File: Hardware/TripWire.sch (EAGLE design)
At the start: 50 parts, among them P1 LSP11, P2 LSP11, P3 LSP11, P4 LSP11, P5 LSP11, P6 LSP11, P7 LSP11, X1 GADGETEER-SOCKET

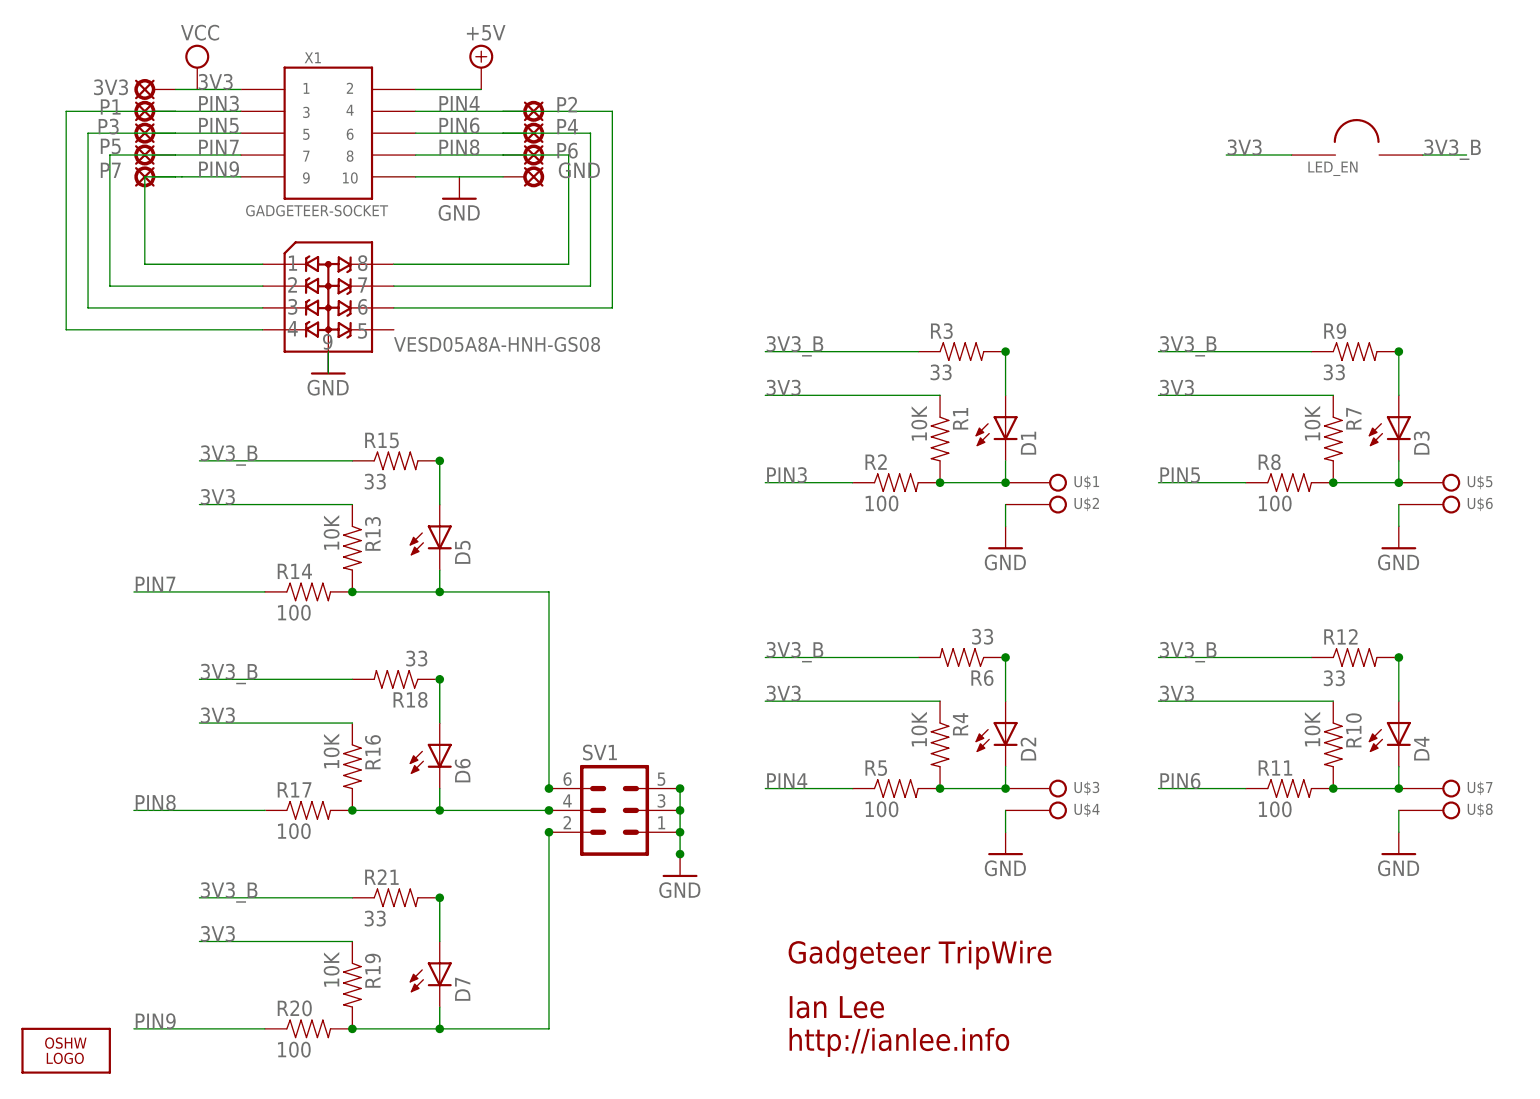
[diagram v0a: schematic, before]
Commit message: Adjusted text sizes & placement.
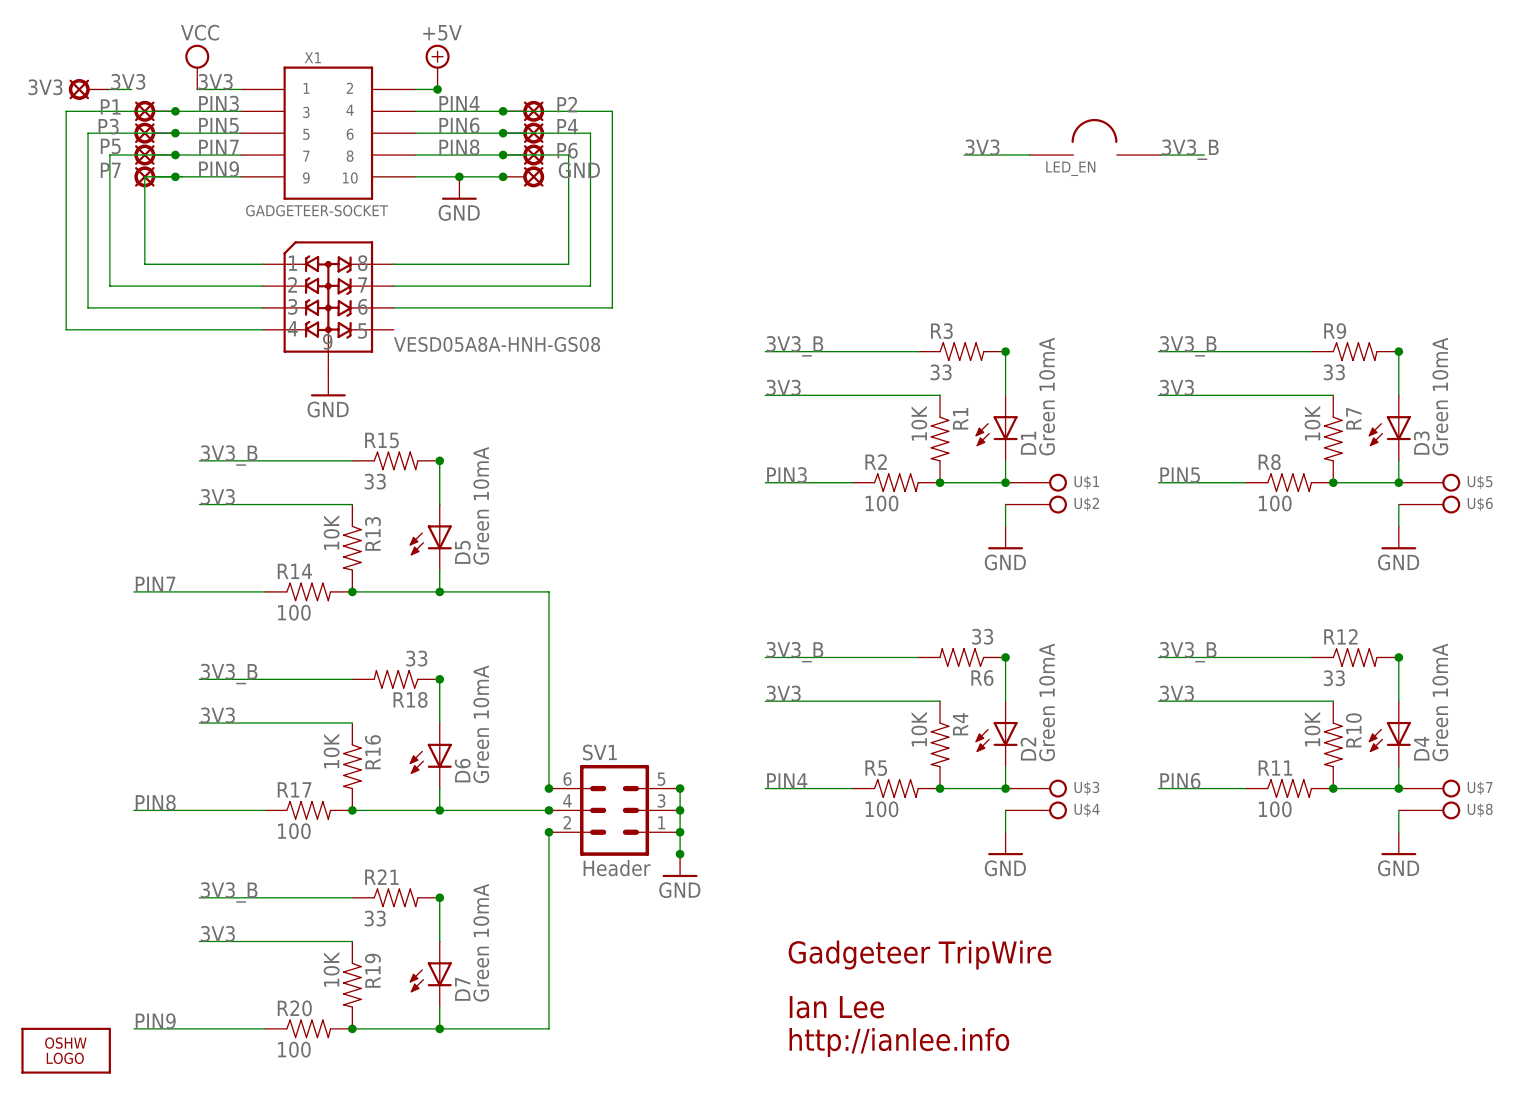
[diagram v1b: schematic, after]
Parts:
- D1, D2, D3, D4, D5, D6, D7: value (none) -> Green 10mA
- SV1: value (none) -> Header
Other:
- moved on the sheet: 3V3, LED_EN
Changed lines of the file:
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@@
 <setting verticaltext="up"/>
 </settings>
-<grid distance="0.1" unitdist="inch" unit="mm" style="lines" multiple="1" display="no" altdistance="0.01" altunitdist="inch" altunit="mm"/>
+<grid distance="0.1" unitdist="inch" unit="inch" style="lines" multiple="1" display="no" altdistance="0.01" altunitdist="inch" altunit="inch"/>
 <layers>
 <layer number="1" name="Top" color="4" fill="1" visible="no" active="no"/>
@@
 </variantdefs>
 <classes>
-<class number="0" name="default" width="0.254" drill="0.381">
+<class number="0" name="default" width="0.1524" drill="0.254">
 <clearance class="0" value="0.2032"/>
 </class>
@@
 <part name="FRAME2" library="frames" deviceset="A5L-LOC" device=""/>
 <part name="GND1" library="supply1" deviceset="GND" device=""/>
-<part name="V1" library="supply2" deviceset="+5V" device=""/>
 <part name="V2" library="supply2" deviceset="VCC" device=""/>
 <part name="X1" library="SoftDust" deviceset="GADGETEER-SOCKET" device=""/>
@@
 <part name="GND5" library="supply1" deviceset="GND" device=""/>
 <part name="GND6" library="supply1" deviceset="GND" device=""/>
-<part name="SV1" library="con-lstb" deviceset="MA03-2" device=""/>
-<part name="D1" library="SparkFun-LED" deviceset="LED-YELLOW" device="0603"/>
+<part name="SV1" library="con-lstb" deviceset="MA03-2" device="" value="Header"/>
+<part name="D1" library="SparkFun-LED" deviceset="LED-YELLOW" device="0603" value="Green 10mA"/>
 <part name="R1" library="SparkFun-Resistors" deviceset="RESISTOR" device="0603-RES" value="10K"/>
 <part name="R2" library="SparkFun-Resistors" deviceset="RESISTOR" device="0603-RES" value="100"/>
 <part name="R3" library="SparkFun-Resistors" deviceset="RESISTOR" device="0603-RES" value="33"/>
-<part name="D2" library="SparkFun-LED" deviceset="LED-YELLOW" device="0603"/>
+<part name="D2" library="SparkFun-LED" deviceset="LED-YELLOW" device="0603" value="Green 10mA"/>
 <part name="R4" library="SparkFun-Resistors" deviceset="RESISTOR" device="0603-RES" value="10K"/>
 <part name="R5" library="SparkFun-Resistors" deviceset="RESISTOR" device="0603-RES" value="100"/>
 <part name="R6" library="SparkFun-Resistors" deviceset="RESISTOR" device="0603-RES" value="33"/>
-<part name="D3" library="SparkFun-LED" deviceset="LED-YELLOW" device="0603"/>
+<part name="D3" library="SparkFun-LED" deviceset="LED-YELLOW" device="0603" value="Green 10mA"/>
 <part name="R7" library="SparkFun-Resistors" deviceset="RESISTOR" device="0603-RES" value="10K"/>
 <part name="R8" library="SparkFun-Resistors" deviceset="RESISTOR" device="0603-RES" value="100"/>
 <part name="R9" library="SparkFun-Resistors" deviceset="RESISTOR" device="0603-RES" value="33"/>
-<part name="D4" library="SparkFun-LED" deviceset="LED-YELLOW" device="0603"/>
+<part name="D4" library="SparkFun-LED" deviceset="LED-YELLOW" device="0603" value="Green 10mA"/>
 <part name="R10" library="SparkFun-Resistors" deviceset="RESISTOR" device="0603-RES" value="10K"/>
 <part name="R11" library="SparkFun-Resistors" deviceset="RESISTOR" device="0603-RES" value="100"/>
 <part name="R12" library="SparkFun-Resistors" deviceset="RESISTOR" device="0603-RES" value="33"/>
-<part name="D5" library="SparkFun-LED" deviceset="LED-YELLOW" device="0603"/>
+<part name="D5" library="SparkFun-LED" deviceset="LED-YELLOW" device="0603" value="Green 10mA"/>
 <part name="R13" library="SparkFun-Resistors" deviceset="RESISTOR" device="0603-RES" value="10K"/>
 <part name="R14" library="SparkFun-Resistors" deviceset="RESISTOR" device="0603-RES" value="100"/>
 <part name="R15" library="SparkFun-Resistors" deviceset="RESISTOR" device="0603-RES" value="33"/>
-<part name="D6" library="SparkFun-LED" deviceset="LED-YELLOW" device="0603"/>
+<part name="D6" library="SparkFun-LED" deviceset="LED-YELLOW" device="0603" value="Green 10mA"/>
 <part name="R16" library="SparkFun-Resistors" deviceset="RESISTOR" device="0603-RES" value="10K"/>
 <part name="R17" library="SparkFun-Resistors" deviceset="RESISTOR" device="0603-RES" value="100"/>
 <part name="R18" library="SparkFun-Resistors" deviceset="RESISTOR" device="0603-RES" value="33"/>
-<part name="D7" library="SparkFun-LED" deviceset="LED-YELLOW" device="0603"/>
+<part name="D7" library="SparkFun-LED" deviceset="LED-YELLOW" device="0603" value="Green 10mA"/>
 <part name="R19" library="SparkFun-Resistors" deviceset="RESISTOR" device="0603-RES" value="10K"/>
 <part name="R20" library="SparkFun-Resistors" deviceset="RESISTOR" device="0603-RES" value="100"/>
@@
 <part name="VESD05A8A-HNH-GS08" library="SoftDust" deviceset="VESD05A8A-HNH-GS08" device="8-UFDFN_TVS-DIODE-ARRAY"/>
 <part name="GND7" library="supply1" deviceset="GND" device=""/>
+<part name="SUPPLY1" library="supply2" deviceset="+5V" device=""/>
 </parts>
 <sheets>
@@
 <instance part="FRAME2" gate="G$1" x="0" y="0"/>
 <instance part="GND1" gate="1" x="55.88" y="106.68"/>
-<instance part="V1" gate="+5V" x="58.42" y="121.92"/>
 <instance part="V2" gate="G$1" x="25.4" y="121.92"/>
 <instance part="X1" gate="G$1" x="40.64" y="114.3" smashed="yes">
@@
 <instance part="R20" gate="G$1" x="38.354" y="10.16"/>
 <instance part="R21" gate="G$1" x="48.514" y="25.4"/>
-<instance part="LED_EN" gate="G$1" x="160.274" y="111.76" smashed="yes">
-<attribute name="NAME" x="154.432" y="109.728" size="1.27" layer="95"/>
+<instance part="LED_EN" gate="G$1" x="129.794" y="111.76" smashed="yes">
+<attribute name="NAME" x="123.952" y="109.728" size="1.27" layer="95"/>
 </instance>
 <instance part="P2" gate="1" x="63.5" y="116.84" smashed="yes" rot="R270">
@@
 <attribute name="NAME" x="67.31" y="109.093" size="1.778" layer="95"/>
 </instance>
-<instance part="3V3" gate="1" x="20.32" y="119.38" smashed="yes" rot="R90">
-<attribute name="NAME" x="17.526" y="120.523" size="1.778" layer="95" rot="R180"/>
+<instance part="3V3" gate="1" x="12.7" y="119.38" smashed="yes" rot="R90">
+<attribute name="NAME" x="9.906" y="120.523" size="1.778" layer="95" rot="R180"/>
 </instance>
 <instance part="P1" gate="1" x="20.32" y="116.84" smashed="yes" rot="R90">
@@
 <attribute name="NAME" x="48.26" y="88.9" size="1.6764" layer="95"/>
 </instance>
-<instance part="GND7" gate="1" x="40.64" y="86.36"/>
+<instance part="GND7" gate="1" x="40.64" y="83.82"/>
+<instance part="SUPPLY1" gate="+5V" x="53.34" y="121.92"/>
 </instances>
 <busses>
@@
 <pinref part="X1" gate="G$1" pin="P$1"/>
 <label x="25.4" y="119.38" size="1.778" layer="95"/>
-<pinref part="3V3" gate="1" pin="MP"/>
 <wire x1="25.4" y1="119.38" x2="30.48" y2="119.38" width="0.1524" layer="91"/>
-<wire x1="22.86" y1="119.38" x2="25.4" y2="119.38" width="0.1524" layer="91"/>
 </segment>
 <segment>
@@
 <segment>
 <pinref part="LED_EN" gate="G$1" pin="P$1"/>
-<wire x1="152.654" y1="111.76" x2="145.034" y2="111.76" width="0.1524" layer="91"/>
-<label x="145.034" y="111.76" size="1.778" layer="95"/>
+<wire x1="122.174" y1="111.76" x2="114.554" y2="111.76" width="0.1524" layer="91"/>
+<label x="114.554" y="111.76" size="1.778" layer="95"/>
+</segment>
+<segment>
+<pinref part="3V3" gate="1" pin="MP"/>
+<wire x1="15.24" y1="119.38" x2="17.78" y2="119.38" width="0.1524" layer="91"/>
+<label x="15.24" y="119.38" size="1.778" layer="95"/>
 </segment>
 </net>
@@
 <pinref part="GND" gate="1" pin="MP"/>
 <wire x1="60.96" y1="109.22" x2="55.88" y2="109.22" width="0.1524" layer="91"/>
+<junction x="55.88" y="109.22"/>
+<junction x="60.96" y="109.22"/>
 </segment>
 <segment>
@@
 <pinref part="GND7" gate="1" pin="GND"/>
 <pinref part="VESD05A8A-HNH-GS08" gate="G$1" pin="P$9"/>
-<wire x1="40.64" y1="86.36" x2="40.64" y2="88.9" width="0.1524" layer="91"/>
-</segment>
-</net>
-<net name="+5V" class="1">
-<segment>
-<wire x1="58.42" y1="119.38" x2="50.8" y2="119.38" width="0.1524" layer="91"/>
-<pinref part="V1" gate="+5V" pin="+5V"/>
-<pinref part="X1" gate="G$1" pin="P$2"/>
 </segment>
 </net>
@@
 <wire x1="10.16" y1="91.44" x2="33.02" y2="91.44" width="0.1524" layer="91"/>
 <pinref part="VESD05A8A-HNH-GS08" gate="G$1" pin="P$4"/>
+<junction x="22.86" y="116.84"/>
 </segment>
 <segment>
@@
 <wire x1="73.66" y1="93.98" x2="48.26" y2="93.98" width="0.1524" layer="91"/>
 <pinref part="VESD05A8A-HNH-GS08" gate="G$1" pin="P$6"/>
+<junction x="60.96" y="116.84"/>
 </segment>
 <segment>
@@
 <wire x1="12.7" y1="114.3" x2="22.86" y2="114.3" width="0.1524" layer="91"/>
 <pinref part="VESD05A8A-HNH-GS08" gate="G$1" pin="P$3"/>
+<junction x="22.86" y="114.3"/>
 </segment>
 <segment>
@@
 <wire x1="15.24" y1="111.76" x2="22.86" y2="111.76" width="0.1524" layer="91"/>
 <pinref part="VESD05A8A-HNH-GS08" gate="G$1" pin="P$2"/>
+<junction x="22.86" y="111.76"/>
 </segment>
 <segment>
@@
 <wire x1="19.304" y1="99.06" x2="19.304" y2="109.22" width="0.1524" layer="91"/>
 <wire x1="19.304" y1="109.22" x2="22.86" y2="109.22" width="0.1524" layer="91"/>
+<junction x="22.86" y="109.22"/>
 </segment>
 <segment>
@@
 <wire x1="71.12" y1="114.3" x2="60.96" y2="114.3" width="0.1524" layer="91"/>
 <pinref part="VESD05A8A-HNH-GS08" gate="G$1" pin="P$7"/>
+<junction x="60.96" y="114.3"/>
 </segment>
 <segment>
@@
 <wire x1="68.58" y1="111.76" x2="60.96" y2="111.76" width="0.1524" layer="91"/>
 <pinref part="VESD05A8A-HNH-GS08" gate="G$1" pin="P$8"/>
+<junction x="60.96" y="111.76"/>
 </segment>
 <segment>
@@
 <segment>
 <pinref part="LED_EN" gate="G$1" pin="P$2"/>
-<wire x1="167.894" y1="111.76" x2="172.974" y2="111.76" width="0.1524" layer="91"/>
-<label x="167.894" y="111.76" size="1.778" layer="95"/>
+<wire x1="137.414" y1="111.76" x2="142.494" y2="111.76" width="0.1524" layer="91"/>
+<label x="137.414" y="111.76" size="1.778" layer="95"/>
 </segment>
 </net>
@@
 </segment>
 </net>
+<net name="+5V" class="0">
+<segment>
+<pinref part="X1" gate="G$1" pin="P$2"/>
+<pinref part="SUPPLY1" gate="+5V" pin="+5V"/>
+<wire x1="50.8" y1="119.38" x2="53.34" y2="119.38" width="0.1524" layer="91"/>
+<junction x="53.34" y="119.38"/>
+</segment>
+</net>
 </nets>
 </sheet>
 </sheets>
+<errors>
+</errors>
 </schematic>
 </drawing>

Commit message: Changed the OSHW logo to use the SparkFun medium one.
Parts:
- LOGO1: value LOGO-OSHW-FILLX0200-NT -> OSHW-LOGOM; device Logo:LOGO-OSHW-FILLX0200-NT -> SparkFun-Aesthetics:OSHW-LOGOM
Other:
- moved on the sheet: 3V3
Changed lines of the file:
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@@
 <part name="V2" library="supply2" deviceset="VCC" device=""/>
 <part name="X1" library="SoftDust" deviceset="GADGETEER-SOCKET" device=""/>
-<part name="LOGO1" library="Logo" deviceset="LOGO-OSHW-FILL" device="X0200-NT"/>
 <part name="U$1" library="SoftDust" deviceset="SPADE-TERMINAL" device="PTH"/>
 <part name="U$2" library="SoftDust" deviceset="SPADE-TERMINAL" device="PTH"/>
@@
 <part name="GND7" library="supply1" deviceset="GND" device=""/>
 <part name="SUPPLY1" library="supply2" deviceset="+5V" device=""/>
+<part name="LOGO1" library="SparkFun-Aesthetics" deviceset="OSHW-LOGO" device="M"/>
 </parts>
 <sheets>
@@
 <attribute name="VALUE" x="30.988" y="104.648" size="1.27" layer="96"/>
 </instance>
-<instance part="LOGO1" gate="G$1" x="10.16" y="7.62"/>
 <instance part="U$1" gate="G$1" x="119.38" y="73.66"/>
 <instance part="U$2" gate="G$1" x="119.38" y="71.12"/>
@@
 <attribute name="NAME" x="67.31" y="109.093" size="1.778" layer="95"/>
 </instance>
-<instance part="3V3" gate="1" x="12.7" y="119.38" smashed="yes" rot="R90">
-<attribute name="NAME" x="9.906" y="120.523" size="1.778" layer="95" rot="R180"/>
+<instance part="3V3" gate="1" x="20.32" y="119.38" smashed="yes" rot="R90">
+<attribute name="NAME" x="17.526" y="120.523" size="1.778" layer="95" rot="R180"/>
 </instance>
 <instance part="P1" gate="1" x="20.32" y="116.84" smashed="yes" rot="R90">
@@
 <instance part="GND7" gate="1" x="40.64" y="83.82"/>
 <instance part="SUPPLY1" gate="+5V" x="53.34" y="121.92"/>
+<instance part="LOGO1" gate="G$1" x="167.64" y="121.92"/>
 </instances>
 <busses>
@@
 <label x="25.4" y="119.38" size="1.778" layer="95"/>
 <wire x1="25.4" y1="119.38" x2="30.48" y2="119.38" width="0.1524" layer="91"/>
+<pinref part="3V3" gate="1" pin="MP"/>
+<label x="25.4" y="119.38" size="1.778" layer="95"/>
+<wire x1="22.86" y1="119.38" x2="25.4" y2="119.38" width="0.1524" layer="91"/>
+<junction x="22.86" y="119.38"/>
 </segment>
 <segment>
@@
 <label x="114.554" y="111.76" size="1.778" layer="95"/>
 </segment>
-<segment>
-<pinref part="3V3" gate="1" pin="MP"/>
-<wire x1="15.24" y1="119.38" x2="17.78" y2="119.38" width="0.1524" layer="91"/>
-<label x="15.24" y="119.38" size="1.778" layer="95"/>
-</segment>
 </net>
